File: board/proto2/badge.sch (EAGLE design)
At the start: 68 parts, among them IC1 TLV62569, J1 5051101092, J2 M05X2X1.27, U1 BMD-300

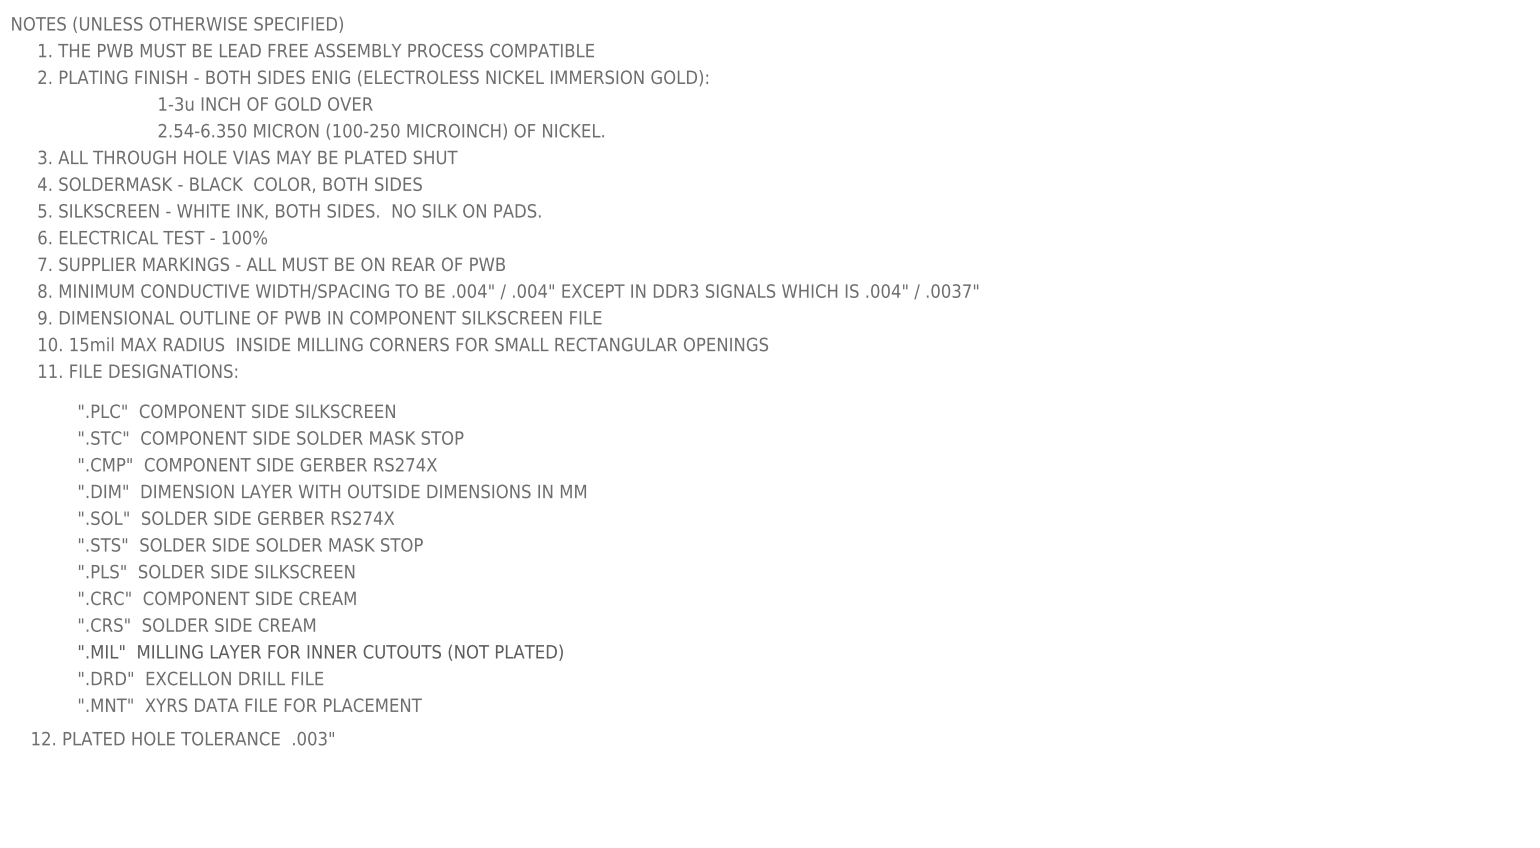
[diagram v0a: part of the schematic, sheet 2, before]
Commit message: update assembly instructions for PCB
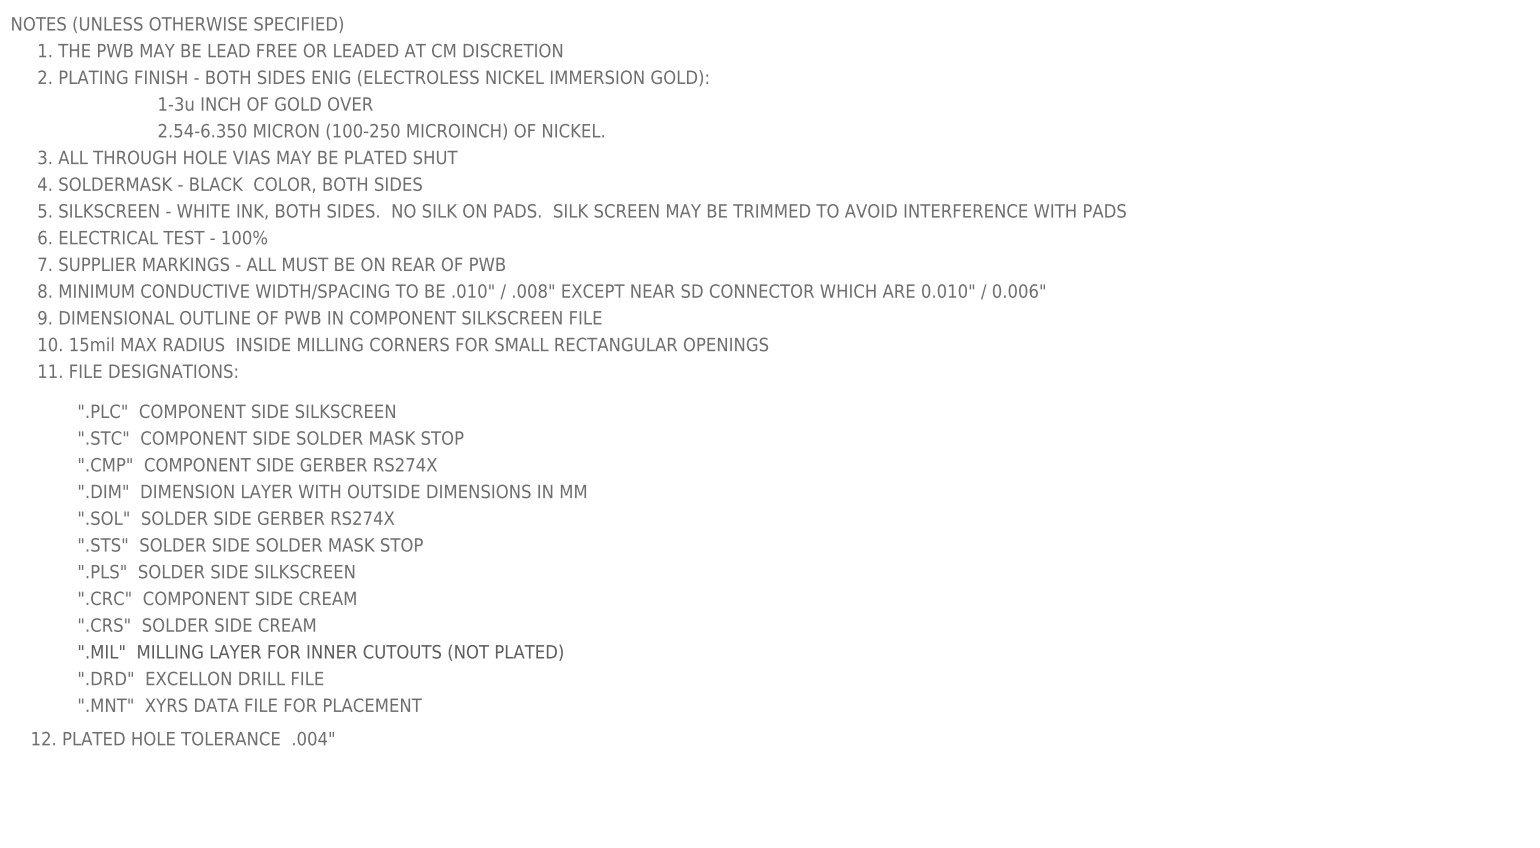
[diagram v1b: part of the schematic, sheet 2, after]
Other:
- note added: "1. THE PWB MAY BE LEAD FREE OR LEADED AT CM DISCRETION"
- note added: "12. PLATED HOLE TOLERANCE .004""
- note added: "5. SILKSCREEN - WHITE INK, BOTH SIDES. NO SILK ON PADS. SILK SCREEN MAY BE TRIMMED TO AVOID INTERFERENCE WITH PADS"
- note added: "8. MINIMUM CONDUCTIVE WIDTH/SPACING TO BE .010" / .008" EXCEPT NEAR SD CONNECTOR WHICH ARE 0.010" / 0.006""
- note removed: "1. THE PWB MUST BE LEAD FREE ASSEMBLY PROCESS COMPATIBLE"
- note removed: "12. PLATED HOLE TOLERANCE .003""
- note removed: "5. SILKSCREEN - WHITE INK, BOTH SIDES. NO SILK ON PADS."
- note removed: "8. MINIMUM CONDUCTIVE WIDTH/SPACING TO BE .004" / .004" EXCEPT IN DDR3 SIGNALS WHICH IS .004" / .0037""

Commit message: WIP schematic rules
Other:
- note added: "4. SOLDERMASK - 250 "A" UNITS WILL HAVE BLACK COLOR, BOTH SIDES, 5 "B" UNITS WILL HAVE RED SOLDERMASK ON BOTH SIDES"
- note removed: "4. SOLDERMASK - BLACK COLOR, BOTH SIDES"
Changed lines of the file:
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@@
 <text x="40.64" y="243.84" size="2.54" layer="95">2.54-6.350 MICRON (100-250 MICROINCH) OF NICKEL.</text>
 <text x="17.78" y="238.76" size="2.54" layer="95">3. ALL THROUGH HOLE VIAS MAY BE PLATED SHUT</text>
-<text x="17.78" y="233.68" size="2.54" layer="95">4. SOLDERMASK - BLACK  COLOR, BOTH SIDES</text>
+<text x="17.78" y="233.68" size="2.54" layer="95">4. SOLDERMASK - 250 "A" UNITS WILL HAVE BLACK  COLOR, BOTH SIDES, 5 "B" UNITS WILL HAVE RED SOLDERMASK ON BOTH SIDES</text>
 <text x="17.78" y="228.6" size="2.54" layer="95">5. SILKSCREEN - WHITE INK, BOTH SIDES.  NO SILK ON PADS.  SILK SCREEN MAY BE TRIMMED TO AVOID INTERFERENCE WITH PADS</text>
 <text x="17.78" y="223.52" size="2.54" layer="95">6. ELECTRICAL TEST - 100%</text>

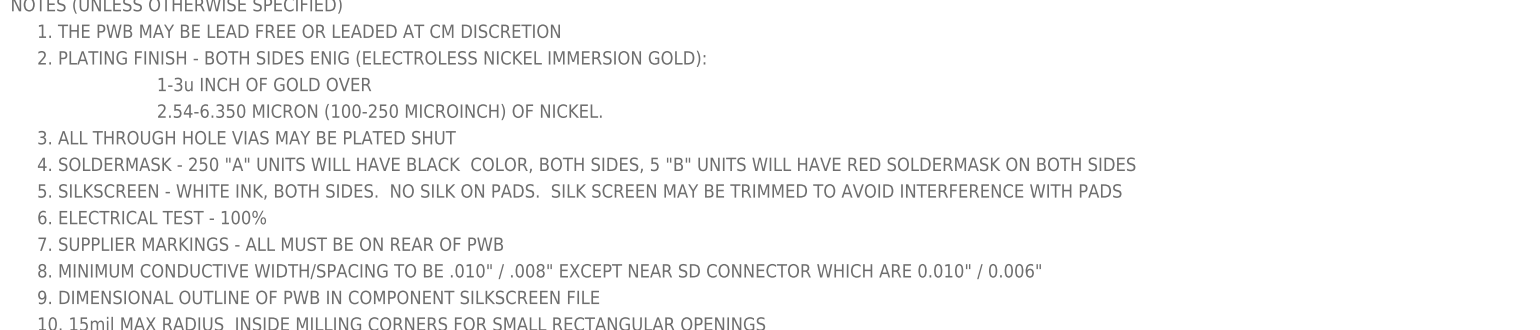
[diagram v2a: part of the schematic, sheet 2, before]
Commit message: change mask to blue for 5 boards
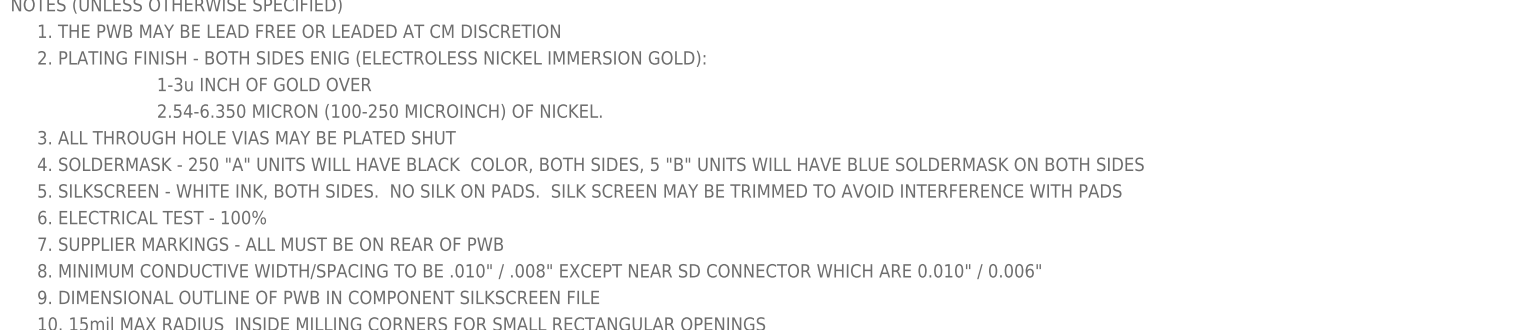
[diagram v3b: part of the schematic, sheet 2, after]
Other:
- note added: "4. SOLDERMASK - 250 "A" UNITS WILL HAVE BLACK COLOR, BOTH SIDES, 5 "B" UNITS WILL HAVE BLUE SOLDERMASK ON BOTH SIDES"
- note removed: "4. SOLDERMASK - 250 "A" UNITS WILL HAVE BLACK COLOR, BOTH SIDES, 5 "B" UNITS WILL HAVE RED SOLDERMASK ON BOTH SIDES"
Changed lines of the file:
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@@
 <text x="40.64" y="243.84" size="2.54" layer="95">2.54-6.350 MICRON (100-250 MICROINCH) OF NICKEL.</text>
 <text x="17.78" y="238.76" size="2.54" layer="95">3. ALL THROUGH HOLE VIAS MAY BE PLATED SHUT</text>
-<text x="17.78" y="233.68" size="2.54" layer="95">4. SOLDERMASK - 250 "A" UNITS WILL HAVE BLACK  COLOR, BOTH SIDES, 5 "B" UNITS WILL HAVE RED SOLDERMASK ON BOTH SIDES</text>
+<text x="17.78" y="233.68" size="2.54" layer="95">4. SOLDERMASK - 250 "A" UNITS WILL HAVE BLACK  COLOR, BOTH SIDES, 5 "B" UNITS WILL HAVE BLUE SOLDERMASK ON BOTH SIDES</text>
 <text x="17.78" y="228.6" size="2.54" layer="95">5. SILKSCREEN - WHITE INK, BOTH SIDES.  NO SILK ON PADS.  SILK SCREEN MAY BE TRIMMED TO AVOID INTERFERENCE WITH PADS</text>
 <text x="17.78" y="223.52" size="2.54" layer="95">6. ELECTRICAL TEST - 100%</text>

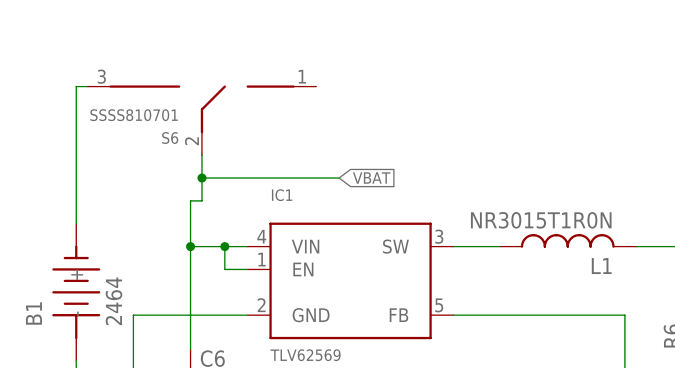
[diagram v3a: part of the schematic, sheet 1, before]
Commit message: swap out switch for one with better mechanical stability
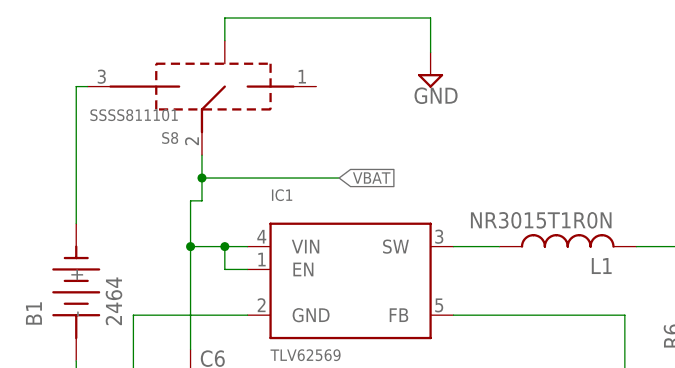
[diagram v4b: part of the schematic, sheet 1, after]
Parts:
- removed S6: SSSS810701, badge:SSSS810701
- added S8: SSSS811101, badge:SSSS811101
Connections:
- net GND: now also S8.GND
- net VBAT: now also S8.2; no longer S6.2
- net VIN: now also S8.3; no longer S6.3
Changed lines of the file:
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@@
 <setting verticaltext="up"/>
 </settings>
-<grid distance="0.1" unitdist="inch" unit="inch" style="lines" multiple="1" display="no" altdistance="0.01" altunitdist="inch" altunit="inch"/>
+<grid distance="0.05" unitdist="inch" unit="inch" style="lines" multiple="1" display="no" altdistance="0.01" altunitdist="inch" altunit="inch"/>
 <layers>
 <layer number="1" name="Top" color="4" fill="1" visible="no" active="no"/>
@@
 <part name="SUPPLY11" library="supply2" deviceset="GND" device=""/>
 <part name="+3V1" library="supply1" deviceset="+3V3" device=""/>
-<part name="S6" library="badge" deviceset="SSSS810701" device=""/>
 <part name="SUPPLY12" library="supply2" deviceset="GND" device=""/>
 <part name="R8" library="rcl" deviceset="R-US_" device="R0603" value="220"/>
@@
 <part name="R11" library="rcl" deviceset="R-US_" device="R0805" value="NP"/>
 <part name="SUPPLY32" library="supply2" deviceset="GND" device=""/>
+<part name="S8" library="badge" deviceset="SSSS811101" device=""/>
+<part name="SUPPLY43" library="supply2" deviceset="GND" device=""/>
 </parts>
 <sheets>
@@
 <attribute name="VALUE" x="172.72" y="115.57" size="1.778" layer="96" rot="R270"/>
 </instance>
-<instance part="S6" gate="G$1" x="36.83" y="264.16" rot="R180"/>
 <instance part="SUPPLY12" gate="GND" x="208.28" y="241.3"/>
 <instance part="R8" gate="G$1" x="165.1" y="236.22" rot="R180"/>
@@
 <instance part="R11" gate="G$1" x="251.46" y="172.72" rot="R90"/>
 <instance part="SUPPLY32" gate="GND" x="251.46" y="165.1"/>
+<instance part="S8" gate="G$1" x="39.37" y="264.16" rot="R180"/>
+<instance part="SUPPLY43" gate="GND" x="62.23" y="265.43"/>
 </instances>
 <busses>
@@
 <pinref part="SUPPLY32" gate="GND" pin="GND"/>
 </segment>
+<segment>
+<pinref part="S8" gate="G$1" pin="GND"/>
+<wire x1="39.37" y1="269.24" x2="39.37" y2="271.78" width="0.1524" layer="91"/>
+<wire x1="39.37" y1="271.78" x2="62.23" y2="271.78" width="0.1524" layer="91"/>
+<wire x1="62.23" y1="271.78" x2="62.23" y2="267.97" width="0.1524" layer="91"/>
+<pinref part="SUPPLY43" gate="GND" pin="GND"/>
+</segment>
 </net>
 <net name="VIN" class="0">
 <segment>
-<pinref part="S6" gate="G$1" pin="3"/>
 <wire x1="22.86" y1="248.92" x2="22.86" y2="264.16" width="0.1524" layer="91"/>
-<wire x1="22.86" y1="264.16" x2="24.13" y2="264.16" width="0.1524" layer="91"/>
 <pinref part="B1" gate="G$1" pin="+"/>
+<pinref part="S8" gate="G$1" pin="3"/>
+<wire x1="24.13" y1="264.16" x2="22.86" y2="264.16" width="0.1524" layer="91"/>
 </segment>
 </net>
@@
 <segment>
 <pinref part="IC1" gate="G$1" pin="VIN"/>
-<wire x1="36.83" y1="256.54" x2="36.83" y2="254" width="0.1524" layer="91"/>
 <wire x1="36.83" y1="254" x2="36.83" y2="251.46" width="0.1524" layer="91"/>
 <wire x1="36.83" y1="251.46" x2="35.56" y2="251.46" width="0.1524" layer="91"/>
@@
 <wire x1="35.56" y1="234.95" x2="35.56" y2="246.38" width="0.1524" layer="91"/>
 <junction x="35.56" y="246.38"/>
-<pinref part="S6" gate="G$1" pin="2"/>
 <wire x1="36.83" y1="254" x2="52.07" y2="254" width="0.1524" layer="91"/>
 <junction x="36.83" y="254"/>
 <label x="52.07" y="254" size="1.27" layer="91" xref="yes"/>
-</segment>
-<segment>
+<pinref part="S8" gate="G$1" pin="2"/>
+<wire x1="36.83" y1="256.54" x2="36.83" y2="254" width="0.1524" layer="91"/>
+</segment>
+<segment>
